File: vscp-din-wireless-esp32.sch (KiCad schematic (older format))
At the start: 17 parts, among them J1 Conn_Left_I2C, J2 Conn_Right_Power, J3 Conn_01x06, U1 ESP32-WROOM-32D

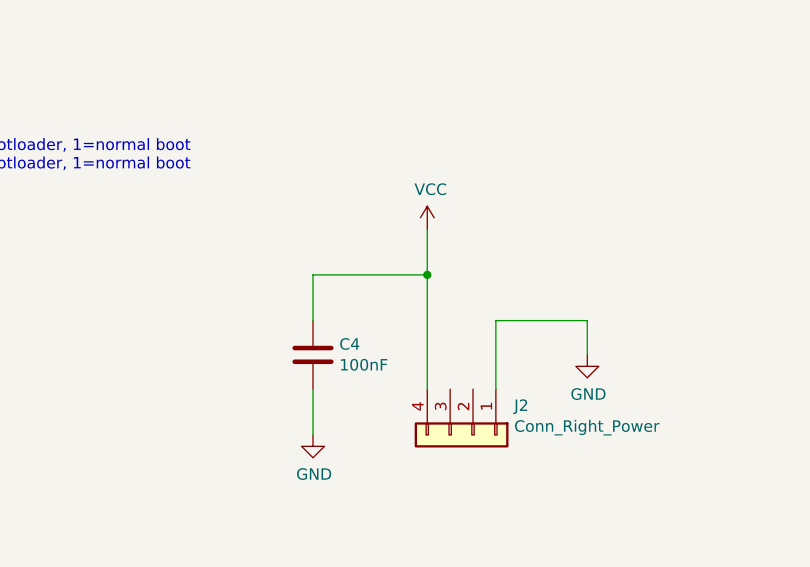
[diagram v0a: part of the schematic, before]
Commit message: Fixed board to board connector
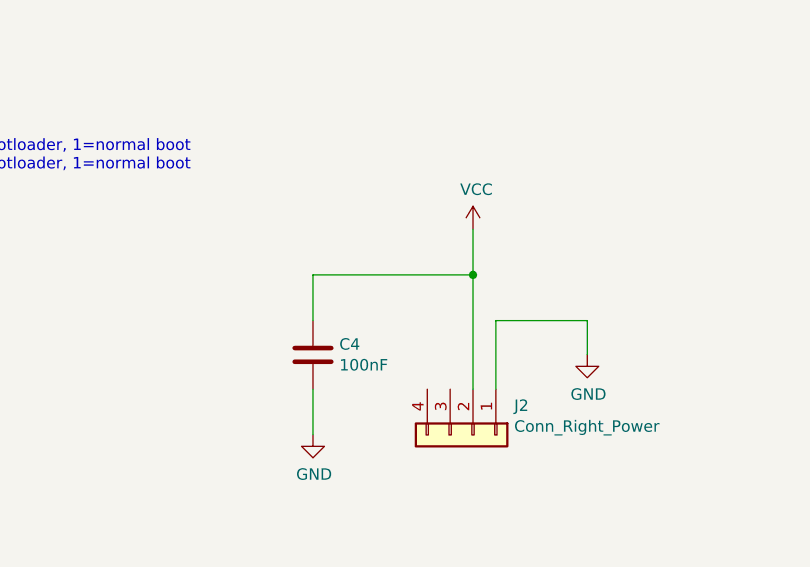
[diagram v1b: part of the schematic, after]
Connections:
- net VCC: now also J2.2 (Pin_2); no longer J2.4 (Pin_4)
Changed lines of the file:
@@
 L power:VCC #PWR0117
 U 1 1 60B3F833
-P 5950 4850
-F 0 "#PWR0117" H 5950 4700 50  0001 C CNN
-F 1 "VCC" H 5965 5023 50  0000 C CNN
-F 2 "" H 5950 4850 50  0001 C CNN
-F 3 "" H 5950 4850 50  0001 C CNN
-	1    5950 4850
-	1    0    0    -1
-$EndComp
-Wire Wire Line
-	5950 5550 5950 5050
+P 6150 4850
+F 0 "#PWR0117" H 6150 4700 50  0001 C CNN
+F 1 "VCC" H 6165 5023 50  0000 C CNN
+F 2 "" H 6150 4850 50  0001 C CNN
+F 3 "" H 6150 4850 50  0001 C CNN
+	1    6150 4850
+	1    0    0    -1
+$EndComp
 $Comp
 L power:GND #PWR0118
@@
 Wire Wire Line
 	5450 5250 5450 5050
-Wire Wire Line
-	5450 5050 5950 5050
-Connection ~ 5950 5050
-Wire Wire Line
-	5950 5050 5950 4850
 $Comp
 L Device:R_Small R4
@@
 Wire Wire Line
 	9900 5400 10150 5400
+Wire Wire Line
+	6150 4850 6150 5050
+Wire Wire Line
+	5450 5050 6150 5050
+Connection ~ 6150 5050
+Wire Wire Line
+	6150 5050 6150 5550
 $EndSCHEMATC

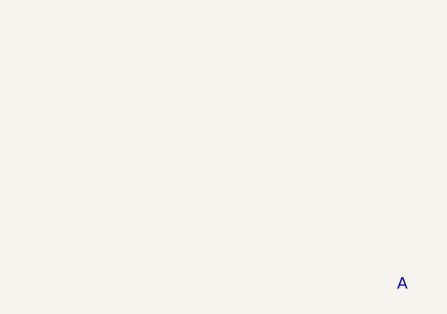
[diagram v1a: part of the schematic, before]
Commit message: srinked board to fit enclosure
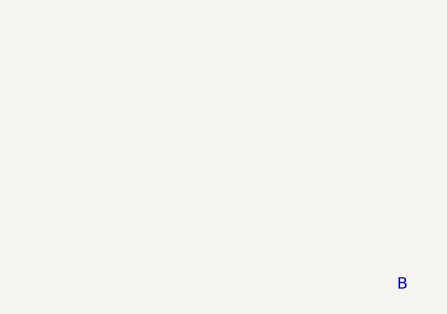
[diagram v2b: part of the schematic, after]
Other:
- note added: "B"
- note removed: "A"
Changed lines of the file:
@@
 VCSP DIN Wireless P1\nCopyright © Åke Hedman, Grodans Paradis AB\nhttps://www.grodansparadis.com\nhttps://www.vscp.org
 Text Notes 10600 7650 0    50   ~ 0
-A
+B
 Text Notes 8100 7650 0    50   ~ 0
 2021-05-20
